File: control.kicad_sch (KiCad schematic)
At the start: 40 parts, among them J5 MCU disable, J6 TC2030, J7 I/O, J8 USB-C, U4 RPMH3.3-0.5, U5 ESP32-C3, U6 ECMF02-2AMX6

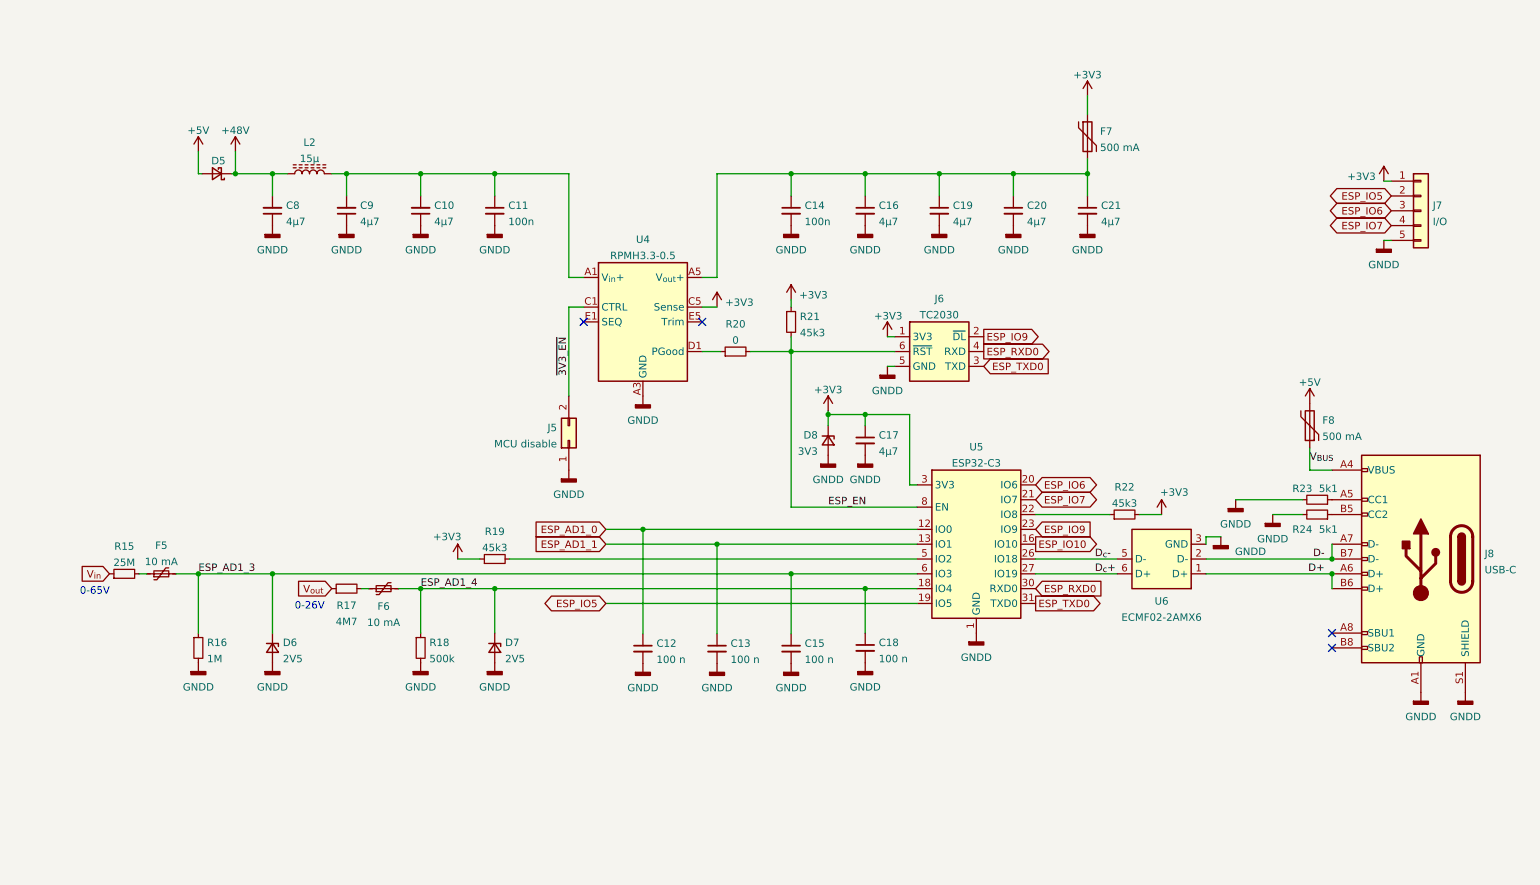
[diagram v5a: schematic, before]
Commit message: Replace generic I/O with LED connector
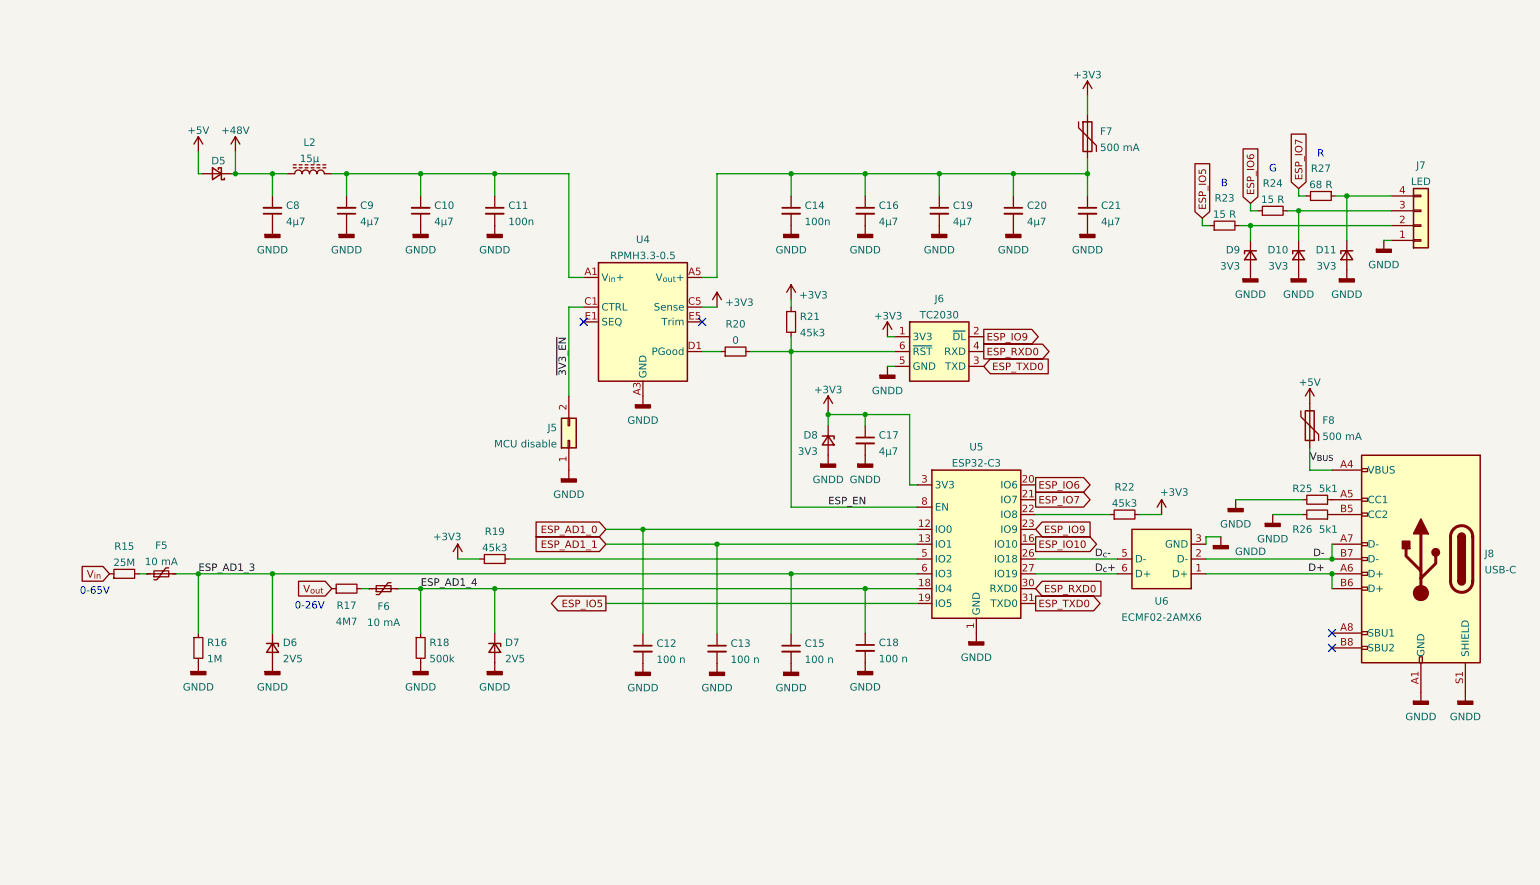
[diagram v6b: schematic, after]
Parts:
- added D10, D11, D9: 3V3, Diode_SMD:D_0402_1005Metric, symbol Device:D_Zener_Small
- added R23, R24: 15 R, Resistor_SMD:R_0603_1608Metric, symbol Device:R_Small
- added R27: 68 R, Resistor_SMD:R_0603_1608Metric, symbol Device:R_Small
- J7: value I/O -> LED; footprint Connector_PinHeader_2.00mm:PinHeader_1x05_P2.00mm_Vertical -> Connector_PinHeader_2.00mm:PinHeader_1x04_P2.00mm_Vertical; symbol Connector_Generic:Conn_01x05 -> Connector_Generic:Conn_01x04; now in the parts list
- renumbered R23 to R25, R24 to R26
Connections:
- net +3V3: no longer J7.1 (Pin_1)
- net ESP_IO5: now also R23.1; no longer J7.2 (Pin_2)
- net ESP_IO6: now also R24.1; no longer J7.3 (Pin_3)
- net ESP_IO7: now also R27.2; no longer J7.4 (Pin_4)
- net GND: now also J7.1 (Pin_1), D10.2 (A), D11.2 (A), D9.2 (A); no longer J7.5 (Pin_5)
- new net: D10.1 (K), J7.3 (Pin_3), R24.2
- new net: D9.1 (K), J7.2 (Pin_2), R23.2
- new net: D11.1 (K), J7.4 (Pin_4), R27.1
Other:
- note added: "B"
- note added: "G"
- note added: "R"

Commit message: Replace resistors with available variants
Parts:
- added R16: 5M, Resistor_SMD:R_1206_3216Metric, symbol Device:R_Small
- added R17: 2M4, Resistor_SMD:R_1206_3216Metric, symbol Device:R_Small
- D6: Part Number UCLAMP2501T.TCT -> UCLAMP2501T.TCT
- R15: value 25M -> 5M; footprint Resistor_SMD:R_0603_1608Metric -> Resistor_SMD:R_1206_3216Metric
- R18: renamed from R16; value 1M -> 499 k; footprint Resistor_SMD:R_0603_1608Metric -> Resistor_SMD:R_0805_2012Metric
- R19: renamed from R17; footprint Resistor_SMD:R_0603_1608Metric -> Resistor_SMD:R_1206_3216Metric
- R20: renamed from R18; value 500k -> 499k; footprint Resistor_SMD:R_0603_1608Metric -> Resistor_SMD:R_0805_2012Metric
- R21: renamed from R19; footprint Resistor_SMD:R_0603_1608Metric -> Resistor_SMD:R_0402_1005Metric
- R22: renamed from R20; value 0 -> 10 m; footprint Resistor_SMD:R_0603_1608Metric -> Resistor_SMD:R_0805_2012Metric
- R23: renamed from R21; footprint Resistor_SMD:R_0603_1608Metric -> Resistor_SMD:R_0402_1005Metric
- R24: renamed from R22; footprint Resistor_SMD:R_0603_1608Metric -> Resistor_SMD:R_0402_1005Metric
- R25: renamed from R23; footprint Resistor_SMD:R_0603_1608Metric -> Resistor_SMD:R_0402_1005Metric
- R26: renamed from R24; footprint Resistor_SMD:R_0603_1608Metric -> Resistor_SMD:R_0402_1005Metric
- R27: renamed from R25; footprint Resistor_SMD:R_0603_1608Metric -> Resistor_SMD:R_0402_1005Metric
- R28: renamed from R26; footprint Resistor_SMD:R_0603_1608Metric -> Resistor_SMD:R_0402_1005Metric
- R29: renamed from R27; footprint Resistor_SMD:R_0603_1608Metric -> Resistor_SMD:R_0402_1005Metric
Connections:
- net ESP_AD1_3: now also R17.2; no longer F5.2
- net ESP_AD1_4: now also R19.2; no longer F6.2
- net V_{in}: now also F5.1; no longer R15.1
- net V_{out}: now also F6.1; no longer R19.1
- net at R15.2: now also R16.1; no longer F5.1
- new net: R16.2, R17.1
- new net: F5.2, R15.1
- new net: F6.2, R19.1
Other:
- moved on the sheet: F5, F6, R15, R19

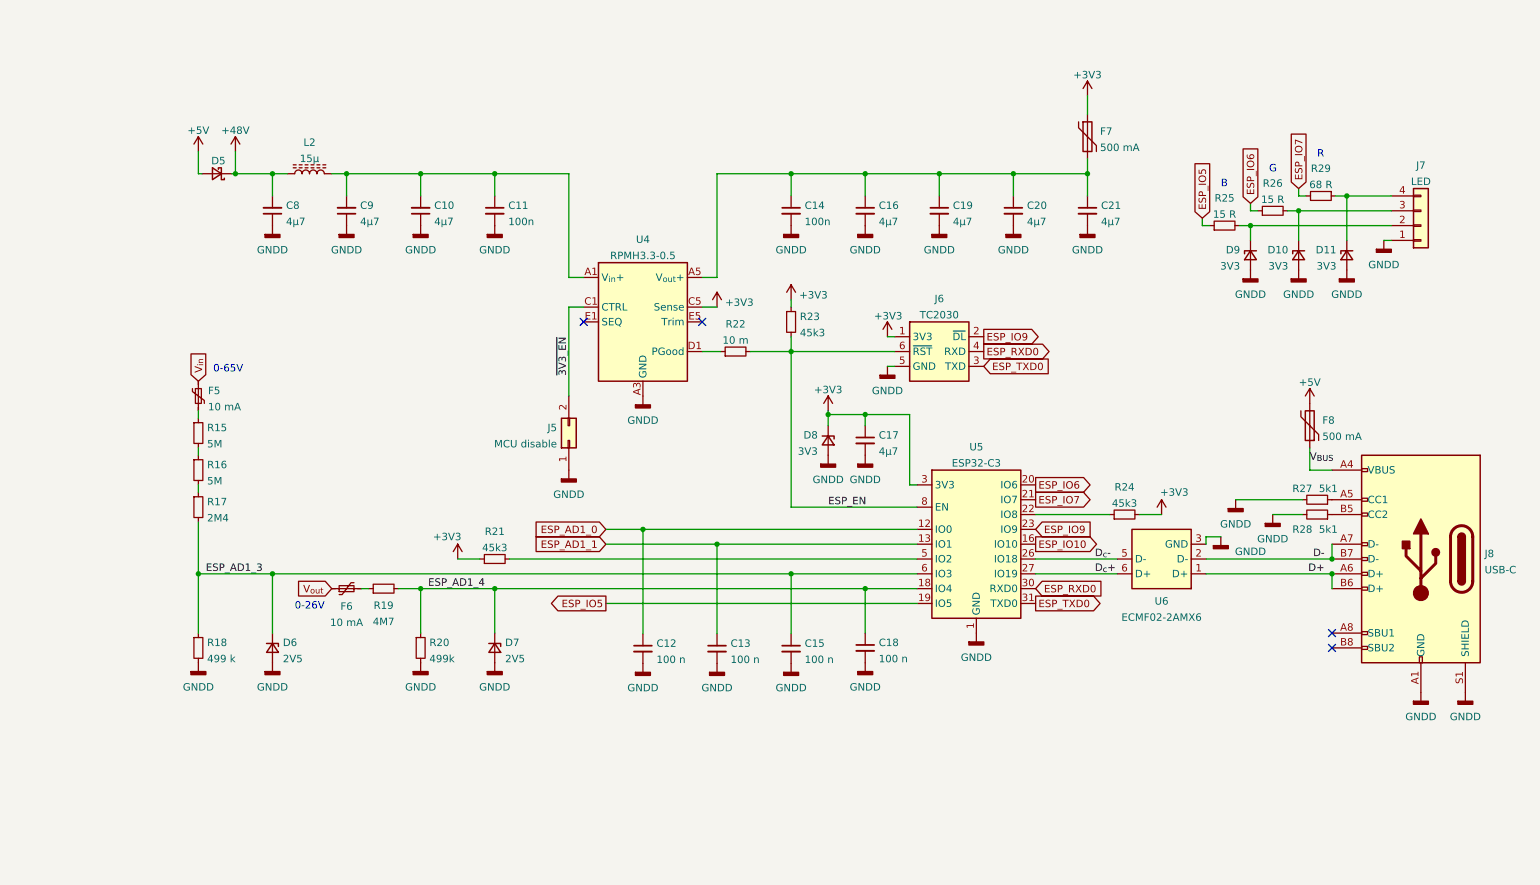
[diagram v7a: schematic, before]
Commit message: Add separate ADCs for remote measurements
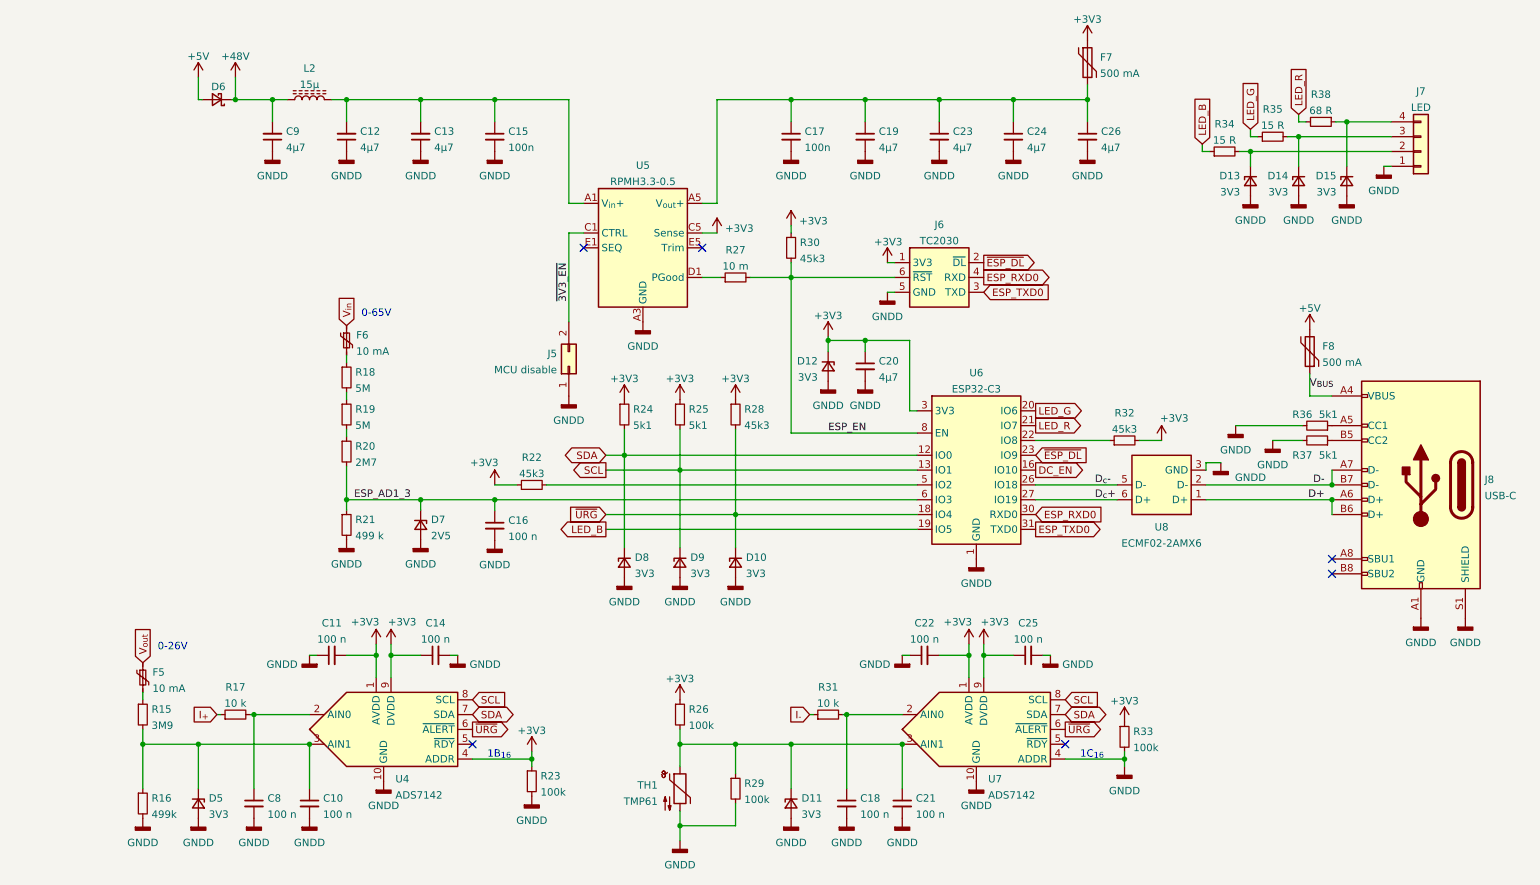
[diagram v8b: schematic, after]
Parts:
- removed C12, C13: 100 n, Capacitor_SMD:C_0402_1005Metric, symbol Device:C_Small
- removed D7: 2V5, Diode_SMD:D_0402_1005Metric, symbol Device:D_Zener_Small
- removed F6: 10 mA, Fuse:Fuse_0603_1608Metric, symbol Device:Polyfuse_Small
- removed R19: 4M7, Resistor_SMD:R_1206_3216Metric, symbol Device:R_Small
- removed R20: 499k, Resistor_SMD:R_0805_2012Metric, symbol Device:R_Small
- added C10, C11, C14, C21, C22, C25, C8: 100 n, Capacitor_SMD:C_0402_1005Metric, symbol Device:C_Small
- added D10, D11, D5, D8, D9: 3V3, Diode_SMD:D_0402_1005Metric, symbol Device:D_Zener_Small
- added F5: 10 mA, Fuse:Fuse_0603_1608Metric, symbol Device:Polyfuse_Small
- added R15: 3M9, Resistor_SMD:R_1206_3216Metric, symbol Device:R_Small
- added R16: 499k, Resistor_SMD:R_0805_2012Metric, symbol Device:R_Small
- added R17, R31: 10 k, Resistor_SMD:R_0402_1005Metric, symbol Device:R_Small
- added R23, R26, R29, R33: 100k, Resistor_SMD:R_0402_1005Metric, symbol Device:R_Small
- added R24, R25: 5k1, Resistor_SMD:R_0402_1005Metric, symbol Device:R_Small
- added R28: 45k3, Resistor_SMD:R_0402_1005Metric, symbol Device:R_Small
- added TH1: TMP61, Resistor_SMD:R_0402_1005Metric, symbol Device:Thermistor_NTC
- added U4, U7: ADS7142, Package_DFN_QFN:Texas_R-PUQFN-N10, symbol phq_IC:ADS7142
- C15: renamed from C11; footprint Capacitor_SMD:C_0402_1005Metric -> Capacitor_SMD:C_0603_1608Metric; Manufacturer Murata -> Taiyo Yuden; Part Number GRM155R72A102KA01J -> HMK107B7104KA
- C17: renamed from C14; Part Number GRM033R71E102KA01E -> GRM155R71E104KE14J
- C18: Manufacturer (none) -> Taiyo Yuden; Part Number (none) -> JMK105B7104KV-F
- L2: Part Number 74404042150 -> 74438356150
- R20: renamed from R17; value 2M4 -> 2M7
- renumbered C9 to C12, C10 to C13, C15 to C16, C16 to C19, C17 to C20, C19 to C23, C20 to C24, C21 to C26, C8 to C9, D8 to D12, D9 to D13, D10 to D14, D11 to D15, D5 to D6, D6 to D7, F5 to F6, R15 to R18, R16 to R19, R18 to R21, R21 to R22, R22 to R27, R23 to R30, R24 to R32, R25 to R34, R26 to R35, R27 to R36, R28 to R37, R29 to R38, U4 to U5, U5 to U6, U6 to U8
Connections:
- net +3V3: now also C11.2, C14.1, C22.2, C25.1, R23.1, R24.1, R25.1, R26.1, R28.1, R33.1, U4.1 (AVDD), U4.4 (ADDR), U4.9 (DVDD), U7.1 (AVDD), U7.9 (DVDD)
- net GND: now also C10.2, C11.1, C14.2, C21.2, C22.1, C25.2, C8.2, D10.2 (A), D11.2 (A), D5.2 (A), D8.2 (A), D9.2 (A), R16.2, R23.2, R29.2, R33.2, TH1.2, U4.10 (GND), U7.10 (GND), U7.4 (ADDR)
- net V_{out}: now also F5.1
- net ESP_AD1_0 renamed SDA
- net SDA: now also D8.1 (K), R24.2, U4.7 (SDA), U7.7 (SDA)
- net ESP_AD1_1 renamed SCL
- net SCL: now also D9.1 (K), R25.2, U4.8 (SCL), U7.8 (SCL)
- net ESP_AD1_4: no longer names the net of C18.1
- net ESP_AD1_4: now also R31.2, U7.2 (AIN0); no longer U6.18 (IO4)
- net ESP_IO10 renamed DC_EN
- net ESP_IO5 renamed LED_B
- net ESP_IO6 renamed LED_G
- net ESP_IO7 renamed LED_R
- net ESP_IO9 renamed ~{ESP_DL}
- new net: C10.1, D5.1 (K), R15.2, R16.1, U4.3 (AIN1)
- new net: C21.1, D11.1 (K), R26.2, R29.1, TH1.1, U7.3 (AIN1)
- new net: F5.2, R15.1
- new net: C8.1, R17.2, U4.2 (AIN0)
- new net I_{+}: R17.1
- new net I_{-}: R31.1
- new net ~{URG}: D10.1 (K), R28.2, U4.6 (~{ALERT}), U6.18 (IO4), U7.6 (~{ALERT})
- no-connect marks 4 -> 6
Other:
- note added: "1B_{16}"
- note added: "1C_{16}"
- note removed: "B"
- note removed: "G"
- note removed: "R"
- moved on the sheet: C12, C13, C15, C16, C17, C19, C20, C23, C24, C26, C9, D12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
